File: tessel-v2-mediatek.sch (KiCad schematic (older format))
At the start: 50 parts, among them J201 CONN_01X01, U201 MT7620N, X201 20MHz

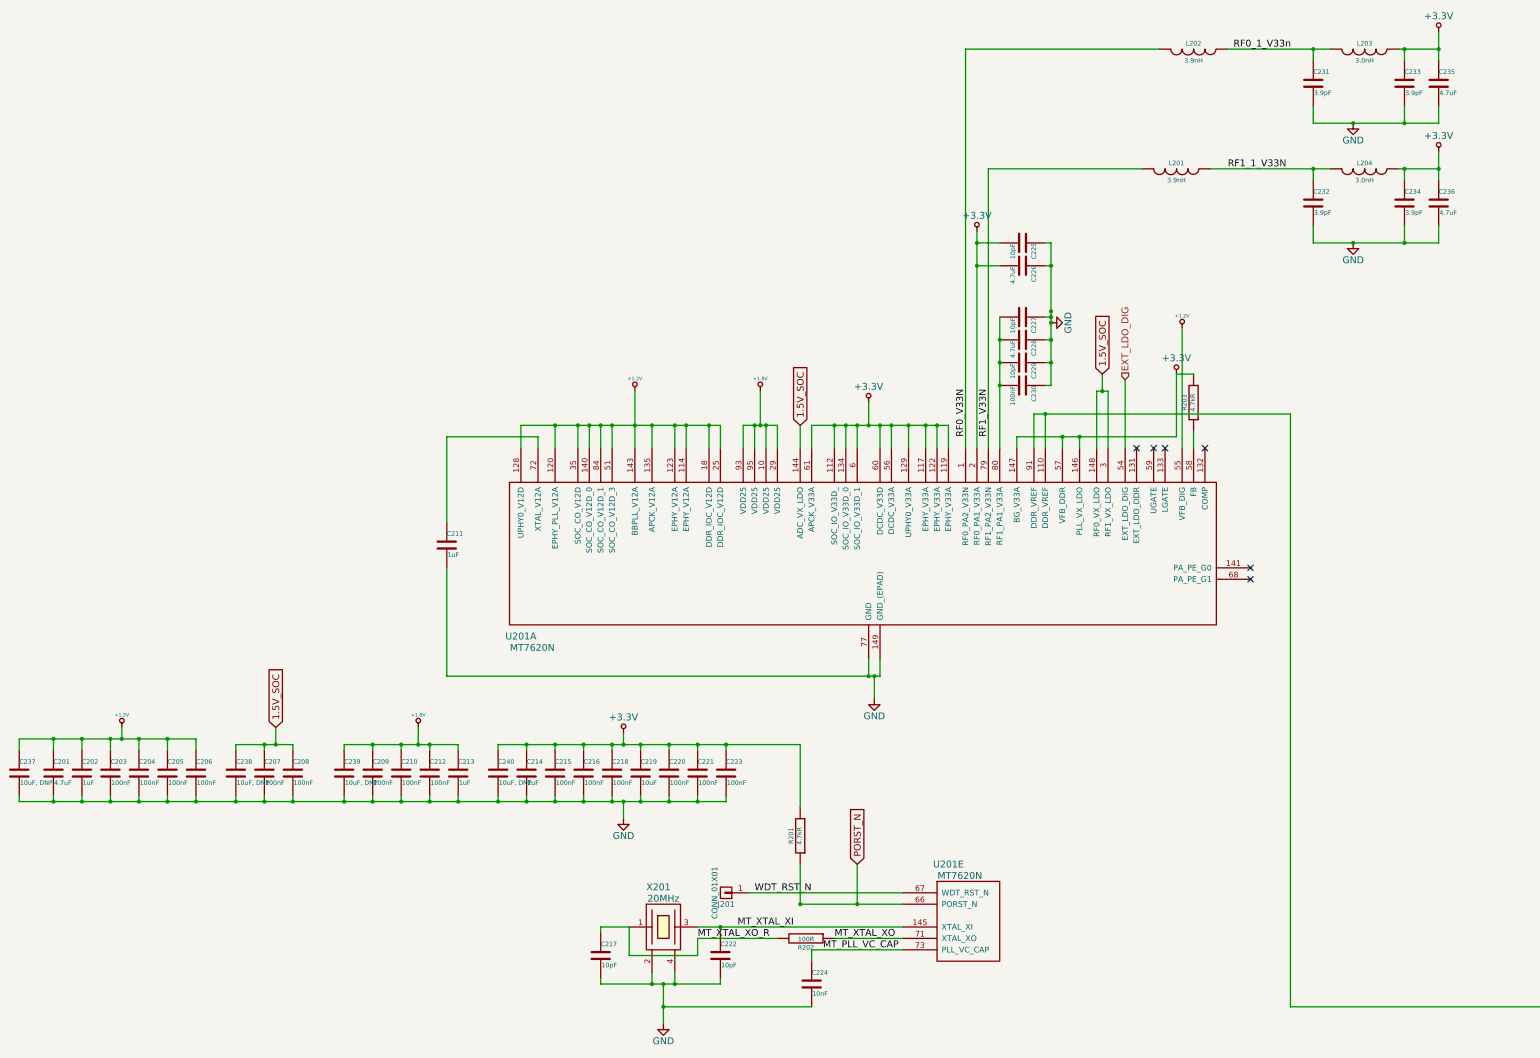
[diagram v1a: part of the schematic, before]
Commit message: apologies jia... needed to re-number things
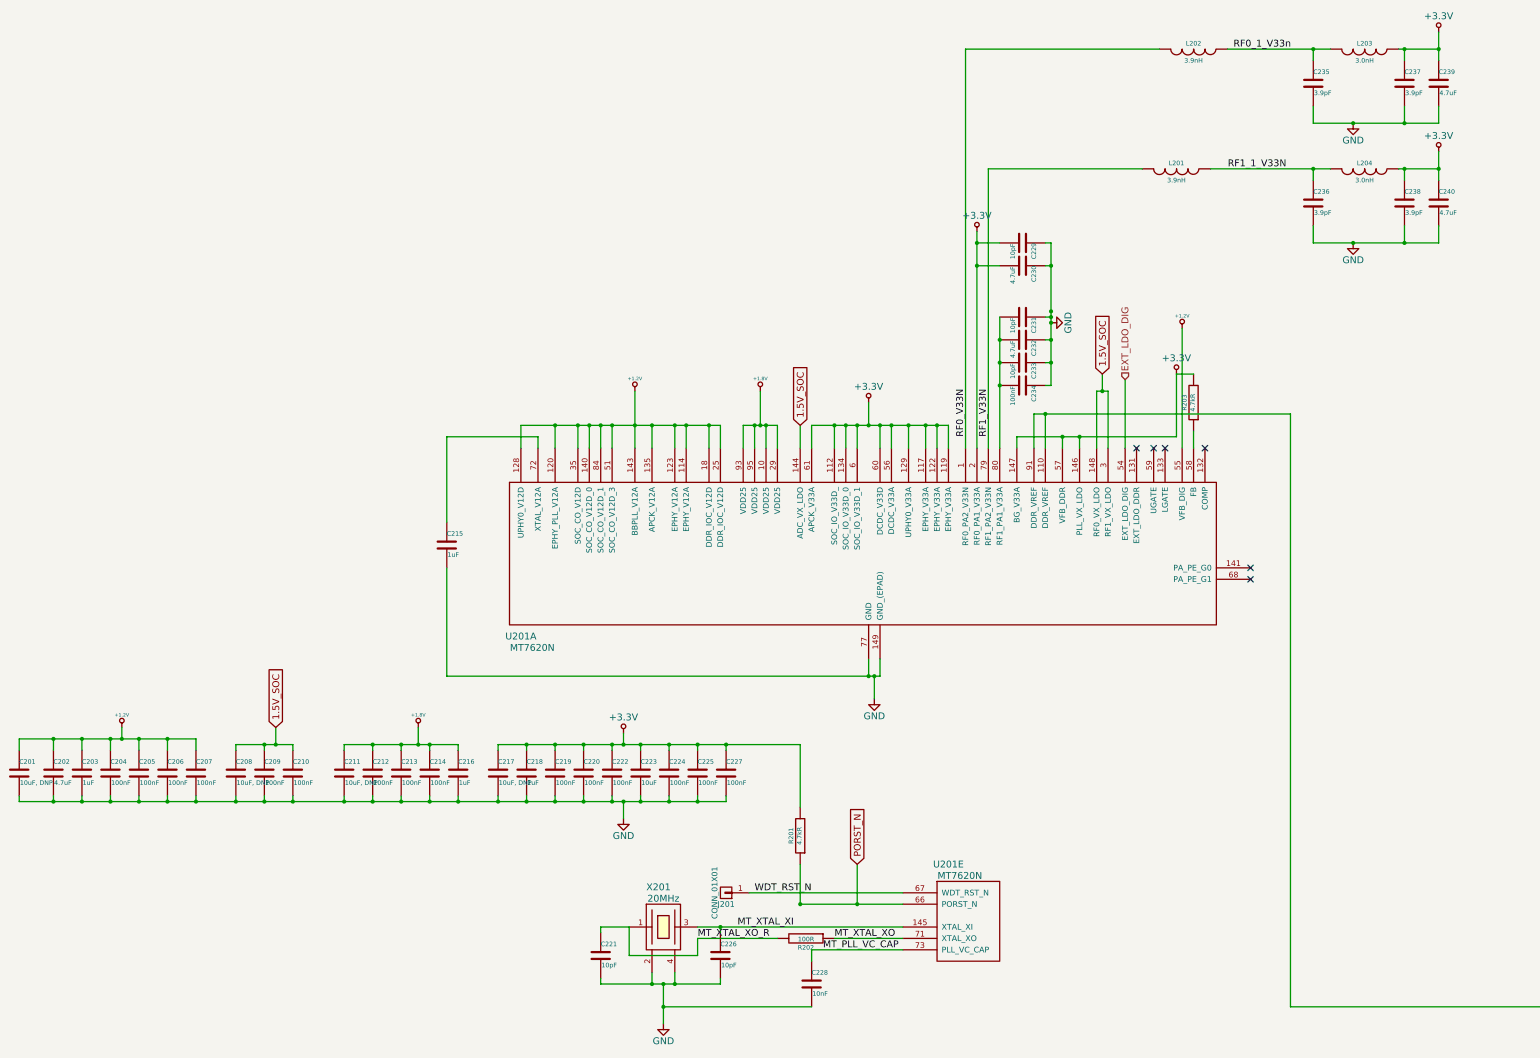
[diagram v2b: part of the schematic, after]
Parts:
- renumbered C237 to C201, C201 to C202, C202 to C203, C203 to C204, C204 to C205, C205 to C206, C206 to C207, C238 to C208, C207 to C209, C208 to C210, C239 to C211, C209 to C212, C210 to C213, C212 to C214, C211 to C215, C213 to C216, C240 to C217, C214 to C218, C215 to C219, C216 to C220, C217 to C221, C218 to C222, C219 to C223, C220 to C224, C221 to C225, C222 to C226, C223 to C227, C224 to C228, C225 to C229, C226 to C230, C227 to C231, C228 to C232, C229 to C233, C230 to C234, C231 to C235, C232 to C236, C233 to C237, C234 to C238, C235 to C239, C236 to C240

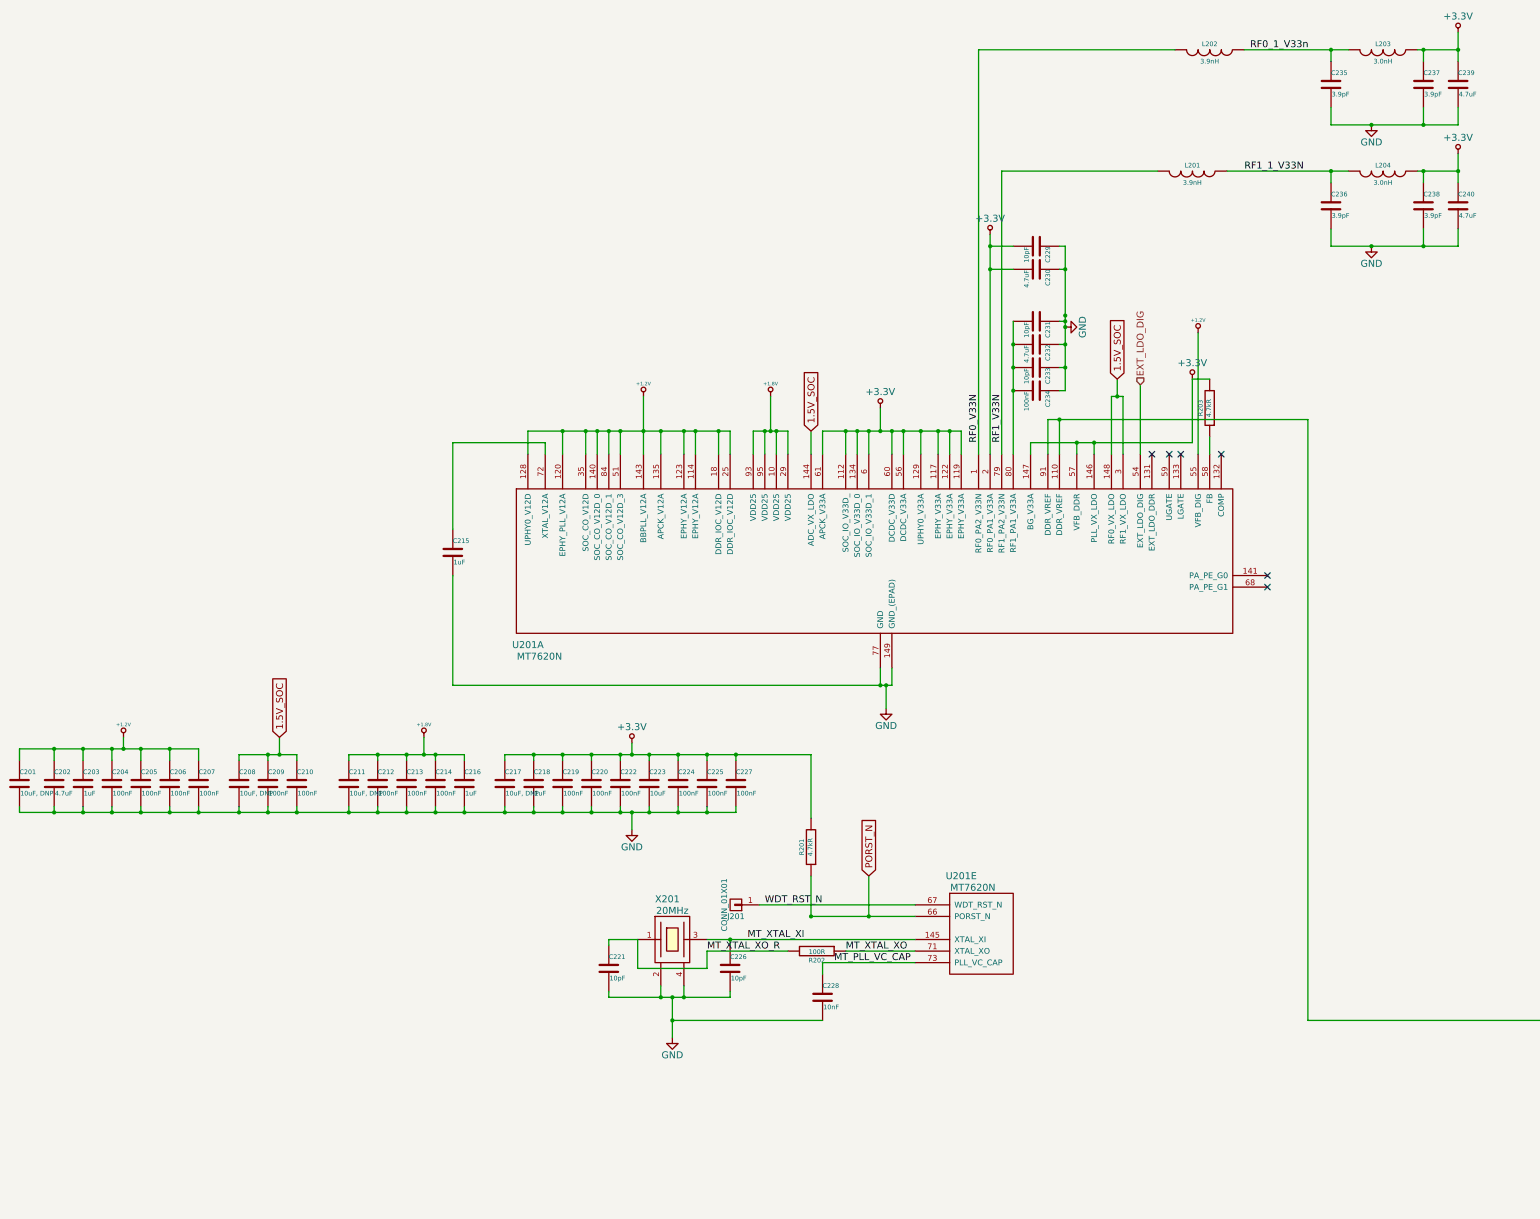
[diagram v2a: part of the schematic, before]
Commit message: swd/jtag pinswaps and LEDs
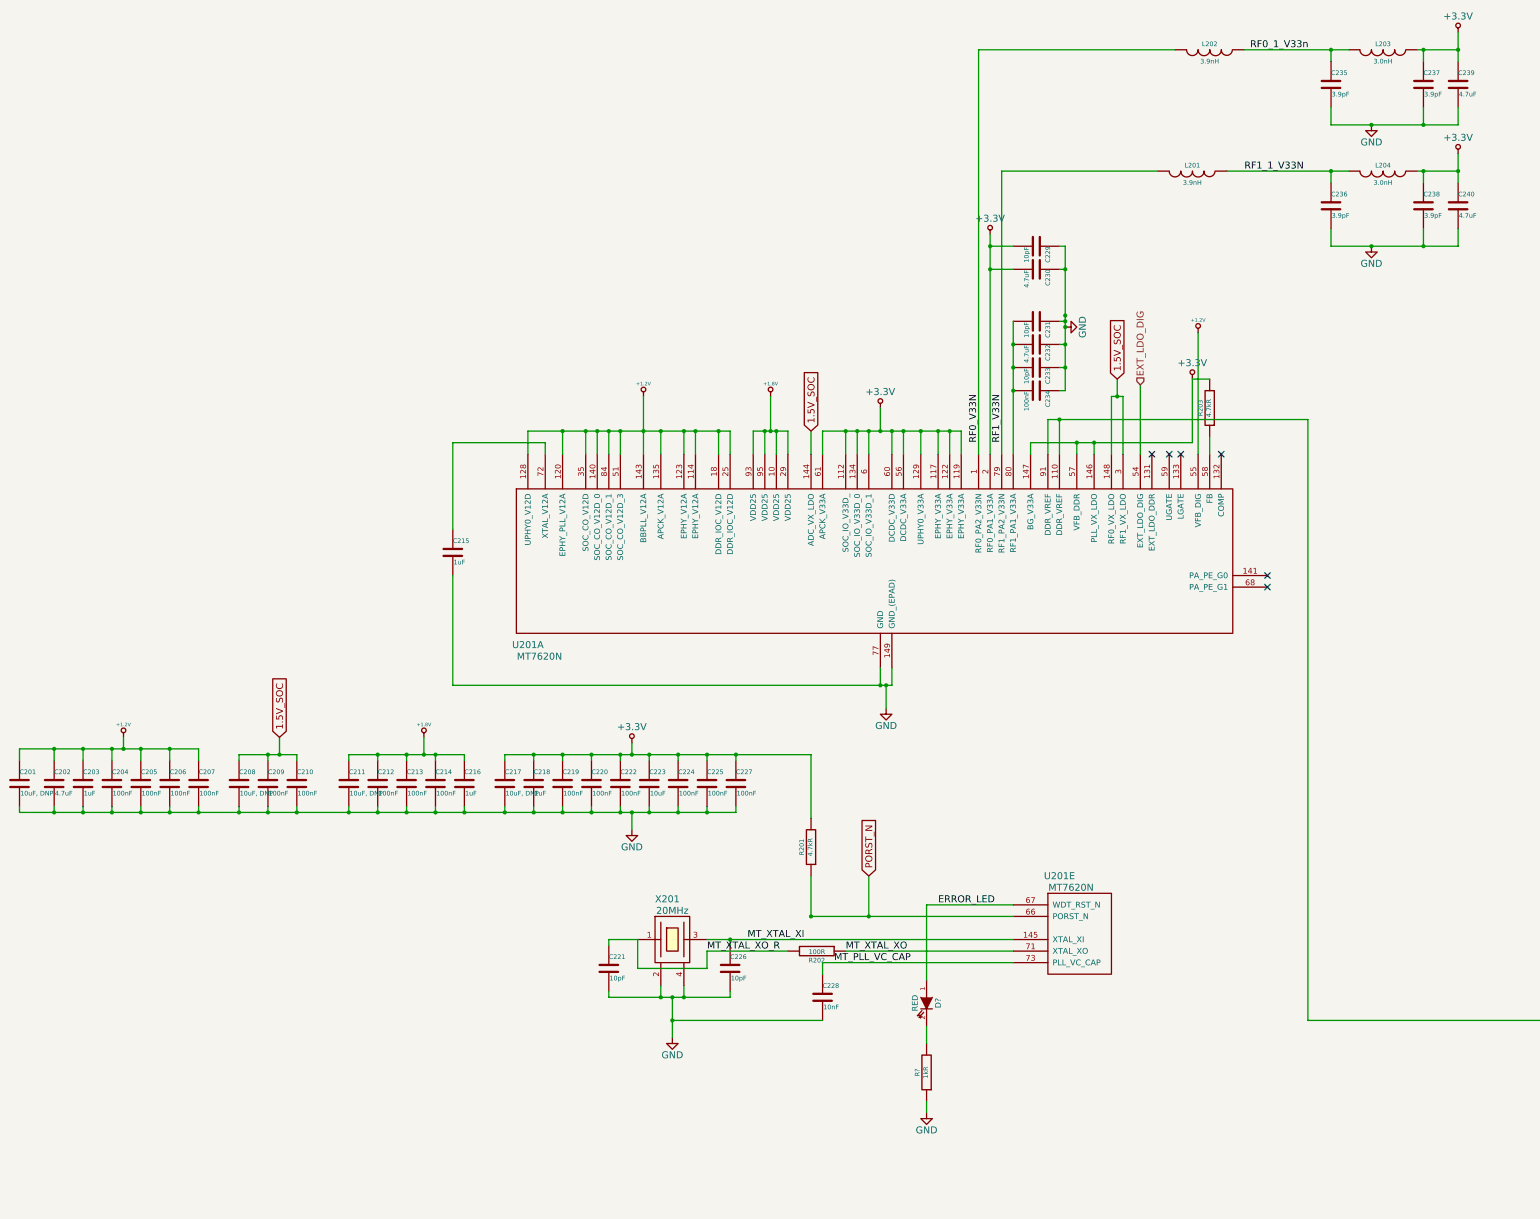
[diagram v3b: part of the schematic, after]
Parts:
- removed J201: CONN_01X01, Pin_Headers:Pin_Header_Straight_1x02, symbol CONN_01X01
- added D?: RED, symbol LED
- added R?: 1kR, tm-kicad-lib:SMD-0402, symbol R
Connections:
- net GND: now also R?.1
- net WDT_RST_N renamed ERROR_LED
- net ERROR_LED: now also D?.1 (A)
- new net: D?.2 (K), R?.2
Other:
- moved on the sheet: U201E

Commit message: re-annotate
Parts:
- gave numbers to parts that had none: 2
- renumbered R203 to R204
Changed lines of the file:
@@
 $EndComp
 $Comp
-L +3.3V #PWR210
+L +3.3V #PWR211
 U 1 1 548FF90D
 P 9450 3850
-F 0 "#PWR210" H 9450 3700 60  0001 C CNN
+F 0 "#PWR211" H 9450 3700 60  0001 C CNN
 F 1 "+3.3V" H 9450 3990 60  0000 C CNN
 F 2 "" H 9450 3850 60  0000 C CNN
@@
 $EndComp
 $Comp
-L GND #PWR211
+L GND #PWR212
 U 1 1 548FFC28
 P 10100 4650
-F 0 "#PWR211" H 10100 4400 60  0001 C CNN
+F 0 "#PWR212" H 10100 4400 60  0001 C CNN
 F 1 "GND" H 10100 4500 60  0000 C CNN
 F 2 "" H 10100 4650 60  0000 C CNN
@@
 NoConn ~ 11450 5750
 $Comp
-L +3.3V #PWR212
+L +3.3V #PWR213
 U 1 1 54901F95
 P 11200 5100
-F 0 "#PWR212" H 11200 4950 60  0001 C CNN
+F 0 "#PWR213" H 11200 4950 60  0001 C CNN
 F 1 "+3.3V" H 11200 5240 60  0000 C CNN
 F 2 "" H 11200 5100 60  0000 C CNN
@@
 $EndComp
 $Comp
-L +3.3V #PWR216
+L +3.3V #PWR217
 U 1 1 5490FE7F
 P 13500 2100
-F 0 "#PWR216" H 13500 1950 60  0001 C CNN
+F 0 "#PWR217" H 13500 1950 60  0001 C CNN
 F 1 "+3.3V" H 13500 2240 60  0000 C CNN
 F 2 "" H 13500 2100 60  0000 C CNN
@@
 $EndComp
 $Comp
-L GND #PWR214
+L GND #PWR215
 U 1 1 54910029
 P 12750 2900
-F 0 "#PWR214" H 12750 2650 60  0001 C CNN
+F 0 "#PWR215" H 12750 2650 60  0001 C CNN
 F 1 "GND" H 12750 2750 60  0000 C CNN
 F 2 "" H 12750 2900 60  0000 C CNN
@@
 $EndComp
 $Comp
-L +3.3V #PWR217
+L +3.3V #PWR218
 U 1 1 54910D64
 P 13500 3150
-F 0 "#PWR217" H 13500 3000 60  0001 C CNN
+F 0 "#PWR218" H 13500 3000 60  0001 C CNN
 F 1 "+3.3V" H 13500 3290 60  0000 C CNN
 F 2 "" H 13500 3150 60  0000 C CNN
@@
 $EndComp
 $Comp
-L GND #PWR215
+L GND #PWR216
 U 1 1 54910D6B
 P 12750 3950
-F 0 "#PWR215" H 12750 3700 60  0001 C CNN
+F 0 "#PWR216" H 12750 3700 60  0001 C CNN
 F 1 "GND" H 12750 3800 60  0000 C CNN
 F 2 "" H 12750 3950 60  0000 C CNN
@@
 $EndComp
 $Comp
-L +1.2V #PWR213
+L +1.2V #PWR214
 U 1 1 5491253A
 P 11250 4700
-F 0 "#PWR213" H 11250 4840 20  0001 C CNN
+F 0 "#PWR214" H 11250 4840 20  0001 C CNN
 F 1 "+1.2V" H 11250 4810 30  0000 C CNN
 F 2 "" H 11250 4700 60  0000 C CNN
@@
 $EndComp
 $Comp
-L R R203
+L R R204
 U 1 1 54912AB6
 P 11350 5350
-F 0 "R203" V 11430 5350 40  0000 C CNN
+F 0 "R204" V 11430 5350 40  0000 C CNN
 F 1 "4.7kR" V 11357 5351 40  0000 C CNN
 F 2 "tm-kicad-lib:SMD-0402" V 11280 5350 30  0001 C CNN
@@
 Connection ~ 5250 8850
 $Comp
-L LED D?
+L LED D201
 U 1 1 54BF4ECE
 P 8900 10500
-F 0 "D?" H 8900 10600 50  0000 C CNN
+F 0 "D201" H 8900 10600 50  0000 C CNN
 F 1 "RED" H 8900 10400 50  0000 C CNN
 F 2 "" H 8900 10500 60  0000 C CNN
@@
 	8900 9650 9650 9650
 $Comp
-L R R?
+L R R203
 U 1 1 54BF5650
 P 8900 11100
-F 0 "R?" V 8980 11100 40  0000 C CNN
+F 0 "R203" V 8980 11100 40  0000 C CNN
 F 1 "1kR" V 8907 11101 40  0000 C CNN
 F 2 "tm-kicad-lib:SMD-0402" V 8830 11100 30  0001 C CNN
@@
 	8900 10850 8900 10700
 $Comp
-L GND #PWR?
+L GND #PWR210
 U 1 1 54BF57E4
 P 8900 11450
-F 0 "#PWR?" H 8900 11200 60  0001 C CNN
+F 0 "#PWR210" H 8900 11200 60  0001 C CNN
 F 1 "GND" H 8900 11300 60  0000 C CNN
 F 2 "" H 8900 11450 60  0000 C CNN
